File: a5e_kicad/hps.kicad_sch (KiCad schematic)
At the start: 4 parts, among them J8 Micro_SD_Card, U13 NXS0506GUX, U7 A5EB013B-B23B

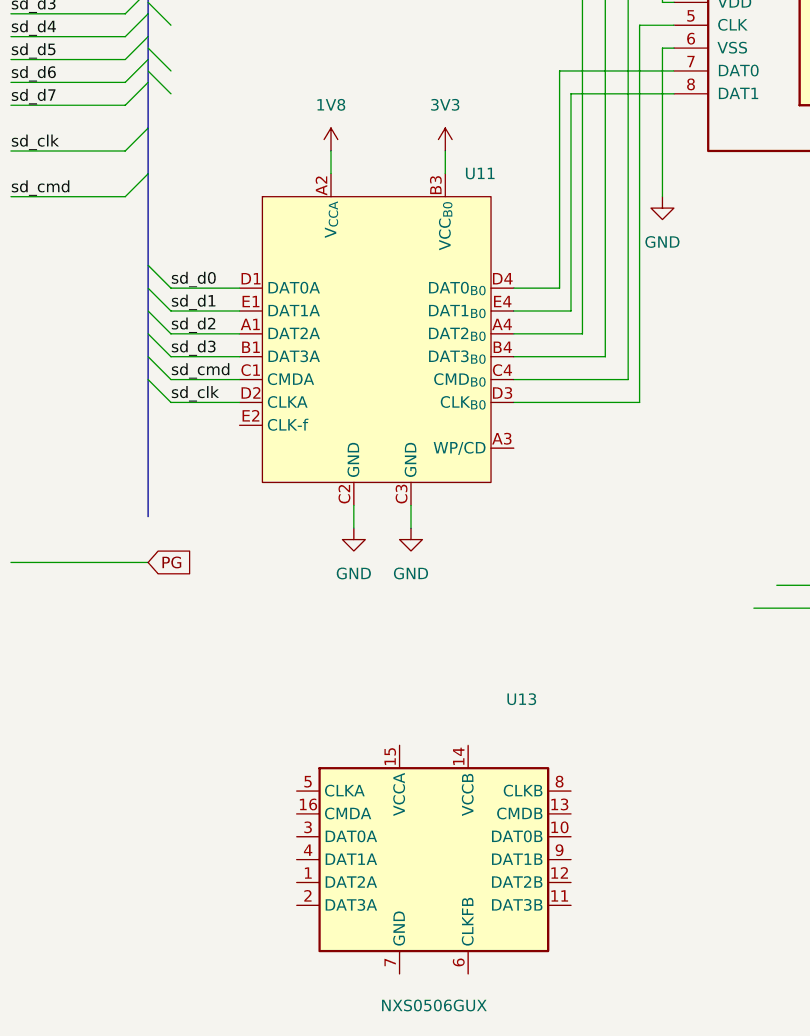
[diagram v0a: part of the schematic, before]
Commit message: fix oscillator supplies and flash pinout, swap SD translator to NXS0506GU
Y2/U9: VDD and GND were reversed - an earlier symbol edit assumed the wrong
schematic pin transform (KiCad subtracts the local Y, it does not add it).
Supplies now land correctly: Y2 VDD->1V8, U9 VDD->3V3, both GND->GND.
U9's enable tie moved from the NC pin to OE.

U2 boot flash: QSPI signals were permuted and VCC/GND were unconnected, from
the same transform error. Re-paired the net labels and moved the 1V8 and GND
symbols onto the VCC/GND pins. All 9 connections verified:
SCLK->qspi_CLK, CS#->~qspi_CS, SIO0-3->qspi_D0-D3, RESET#->~qspi_rst_n.

U11: TXS0206A (DSBGA-20, 0.4mm BGA) -> NXS0506GUX (XQFN16). The new symbol's
pins are placed on the old pin coordinates so every existing schematic
connection carries over; A side on sd_clk/sd_cmd/sd_d0-d3, B side verified
through to the matching J8 pins. Board footprint sits at the same location
and all SD traces are left in place for rerouting.

NXS0506GU footprint corrected to the Nexperia SOT1161-1 reflow pattern:
lands 0.45 x 0.22mm (were 0.35 x 0.20), row centres 1.65mm across the 1.8mm
axis and 2.45mm across the 2.6mm axis (were on the package edge at 1.80 and
2.60). Land span is now 2.10 x 2.90mm, matching the drawing, with an equal
0.15mm outboard extension on both axes. Previously each land overlapped only
the outer third of its terminal.

U13: removed - unwired duplicate of U11.

U7: pad "BF57 " had a trailing space, so the symbol pin did not map to it.

Schematic symbol caches: unit sub-symbol names must not carry the library
prefix (agilex_5_lib:NAME_0_1 -> NAME_0_1), which blocked loading.

Co-Authored-By: Claude Opus 5 <noreply@anthropic.com>
Claude-Session: https://claude.ai/code/session_01DTvSTbyDRanUUYSTEfFpVv
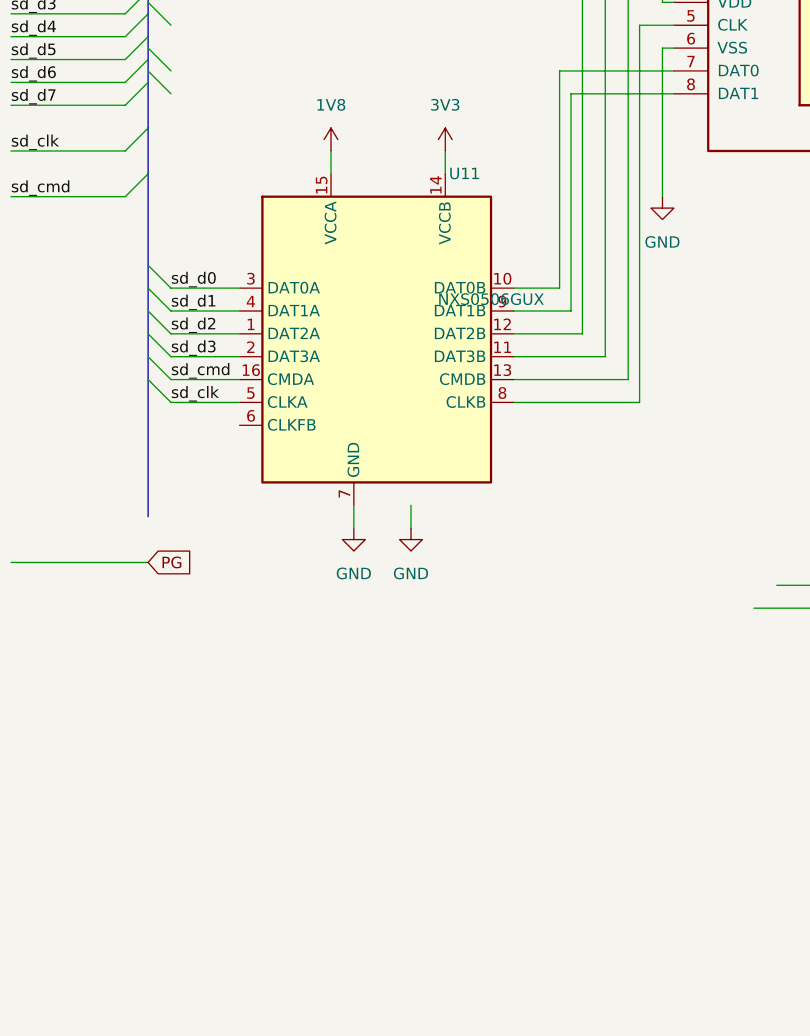
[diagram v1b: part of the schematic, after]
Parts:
- removed U13: NXS0506GUX, agilex_lib:NXS0506GU_XQFN16_1.8x2.6mm_P0.4mm, symbol agilex_5_lib:NXS0506GU
- U11: value (none) -> NXS0506GUX; footprint Package_BGA:Texas_YFP0020_DSBGA-20_1.588x1.988mm_Layout4x5_P0.4mm -> agilex_lib:NXS0506GU_XQFN16_1.8x2.6mm_P0.4mm; symbol agilex_5_lib:TXS0206A -> agilex_5_lib:NXS0506GU
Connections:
- net 1V8: now also U11.15 (VCCA); no longer U11.A2 (V_{CCA})
- net 3V3: now also U11.14 (VCCB); no longer U11.B3 (VCC_{B0})
- net GND: now also U11.7 (GND); no longer U11.C2 (GND), U11.C3 (GND)
- net sd_clk: now also U11.5 (CLKA); no longer U11.D2 (CLKA)
- net sd_cmd: now also U11.16 (CMDA); no longer U11.C1 (CMDA)
- net sd_d0: now also U11.3 (DAT0A); no longer U11.D1 (DAT0A)
- net sd_d1: now also U11.4 (DAT1A); no longer U11.E1 (DAT1A)
- net sd_d2: now also U11.1 (DAT2A); no longer U11.A1 (DAT2A)
- net sd_d3: now also U11.2 (DAT3A); no longer U11.B1 (DAT3A)
- net at J8.1 (DAT2): now also U11.12 (DAT2B); no longer U11.A4 (DAT2_{B0})
- net at J8.2 (DAT3/CD): now also U11.11 (DAT3B); no longer U11.B4 (DAT3_{B0})
- net at J8.3 (CMD): now also U11.13 (CMDB); no longer U11.C4 (CMD_{B0})
- net at J8.5 (CLK): now also U11.8 (CLKB); no longer U11.D3 (CLK_{B0})
- net at J8.7 (DAT0): now also U11.10 (DAT0B); no longer U11.D4 (DAT0_{B0})
- net at J8.8 (DAT1): now also U11.9 (DAT1B); no longer U11.E4 (DAT1_{B0})
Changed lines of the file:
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@@
-	)
-	(symbol
-		(lib_id "agilex_5_lib:NXS0506GU")
-		(at 62.23 158.75 0)
-		(unit 1)
-		(body_style 1)
-		(exclude_from_sim no)
-		(in_bom yes)
-		(on_board yes)
-		(in_pos_files yes)
-		(dnp no)
-		(fields_autoplaced yes)
-		(property "Reference" "U13"
-			(at 71.9933 140.97 0)
-			(show_name no)
-			(do_not_autoplace no)
-			(effects
-				(font
-					(size 1.27 1.27)
-				)
-			)
-		)
-		(property "Value" "NXS0506GUX"
-			(at 62.23 175 0)
-			(show_name no)
-			(do_not_autoplace no)
-			(effects
-				(font
-					(size 1.27 1.27)
-				)
-			)
-		)
-		(property "Footprint" "agilex_lib:NXS0506GU_XQFN16_1.8x2.6mm_P0.4mm"
-			(at 62.23 158.75 0)
-			(hide yes)
-			(show_name no)
-			(do_not_autoplace no)
-			(effects
-				(font
-					(size 1.27 1.27)
-				)
-			)
-		)
-		(property "Datasheet" "https://assets.nexperia.com/documents/data-sheet/NXS0506.pdf"
-			(at 62.23 158.75 0)
-			(hide yes)
-			(show_name no)
-			(do_not_autoplace no)
-			(effects
-				(font
-					(size 1.27 1.27)
-				)
-			)
-		)
-		(property "Description" "SD 3.0 auto-direction 6-channel dual-supply level translator (CLK+CMD+DAT0-3), XQFN16 - no CD/WP passthrough"
-			(at 62.23 158.75 0)
-			(hide yes)
-			(show_name no)
-			(do_not_autoplace no)
-			(effects
-				(font
-					(size 1.27 1.27)
-				)
-			)
-		)
-		(pin "1"
-		)
-		(pin "2"
-		)
-		(pin "3"
-		)
-		(pin "4"
-		)
-		(pin "5"
-		)
-		(pin "6"
-		)
-		(pin "7"
-		)
-		(pin "8"
-		)
-		(pin "9"
-		)
-		(pin "10"
-		)
-		(pin "11"
-		)
-		(pin "12"
-		)
-		(pin "13"
-		)
-		(pin "14"
-		)
-		(pin "15"
-		)
-		(pin "16"
-		)
-		(instances
-			(project "agilex_3_soc"
-				(path "/a5b98d95-6877-4284-904f-d04e32723ae0/1bba180f-a717-40d4-b2d6-e5a7b998021f"
-					(reference "U13")
-					(unit 1)
-				)
-			)
-		)
 	)
 	(symbol
@@
 	)
 	(symbol
-		(lib_id "agilex_5_lib:TXS0206A")
+		(lib_id "agilex_5_lib:NXS0506GU")
 		(at 55.88 100.33 0)
 		(unit 1)
@@
 					(size 1.27 1.27)
 				)
-				(justify left)
-			)
-		)
-		(property "Value" ""
+			)
+		)
+		(property "Value" "NXS0506GUX"
+			(at 68.58 96.52 0)
+			(show_name no)
+			(do_not_autoplace no)
+			(effects
+				(font
+					(size 1.27 1.27)
+				)
+			)
+		)
+		(property "Footprint" "agilex_lib:NXS0506GU_XQFN16_1.8x2.6mm_P0.4mm"
 			(at 55.88 100.33 0)
 			(show_name no)
 			(do_not_autoplace no)
-			(effects
-				(font
-					(size 1.27 1.27)
-				)
-			)
-		)
-		(property "Footprint" "Package_BGA:Texas_YFP0020_DSBGA-20_1.588x1.988mm_Layout4x5_P0.4mm"
+			(hide yes)
+			(effects
+				(font
+					(size 1.27 1.27)
+				)
+			)
+		)
+		(property "Datasheet" "https://assets.nexperia.com/documents/data-sheet/NXS0506.pdf"
 			(at 55.88 100.33 0)
-			(hide yes)
-			(show_name no)
-			(do_not_autoplace no)
-			(effects
-				(font
-					(size 1.27 1.27)
-				)
-			)
-		)
-		(property "Datasheet" ""
+			(show_name no)
+			(do_not_autoplace no)
+			(hide yes)
+			(effects
+				(font
+					(size 1.27 1.27)
+				)
+			)
+		)
+		(property "Description" "SD 3.0 auto-direction 6-channel dual-supply level translator, XQFN16"
 			(at 55.88 100.33 0)
-			(hide yes)
-			(show_name no)
-			(do_not_autoplace no)
-			(effects
-				(font
-					(size 1.27 1.27)
-				)
-			)
-		)
-		(property "Description" ""
-			(at 55.88 100.33 0)
-			(hide yes)
-			(show_name no)
-			(do_not_autoplace no)
-			(effects
-				(font
-					(size 1.27 1.27)
-				)
-			)
-		)
-		(pin "A3"
-		)
-		(pin "A2"
-		)
-		(pin "A1"
-		)
-		(pin "B4"
-		)
-		(pin "C4"
-		)
-		(pin "C3"
-		)
-		(pin "D1"
-		)
-		(pin "D3"
-		)
-		(pin "E1"
-		)
-		(pin "E2"
-		)
-		(pin "A4"
-		)
-		(pin "B3"
-		)
-		(pin "B1"
-		)
-		(pin "C1"
-		)
-		(pin "D4"
-		)
-		(pin "D2"
-		)
-		(pin "C2"
-		)
-		(pin "E4"
-		)
-		(instances
+			(show_name no)
+			(do_not_autoplace no)
+			(hide yes)
+			(effects
+				(font
+					(size 1.27 1.27)
+				)
+			)
+		)
+		(pin "1"
+		)
+		(pin "2"
+		)
+		(pin "3"
+		)
+		(pin "4"
+		)
+		(pin "5"
+		)
+		(pin "6"
+		)
+		(pin "7"
+		)
+		(pin "8"
+		)
+		(pin "9"
+		)
+		(pin "10"
+		)
+		(pin "11"
+		)
+		(pin "12"
+		)
+		(pin "13"
+		)
+		(pin "14"
+		)
+		(pin "15"
+		)
+		(pin "16"
+		)
+		(instances
